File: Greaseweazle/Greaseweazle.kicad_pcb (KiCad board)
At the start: 2 copper layers, 90 x 94 mm, 20 parts, among them J1 FDC_PC, J2 PWR_EXT1, J3 PWR_DRV, J4 PWR_EXT2, J5 USB_TTL, J6 FDC_Amstrad, M1 Mounting, M2 Mounting, M3 Mounting, M4 Mounting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

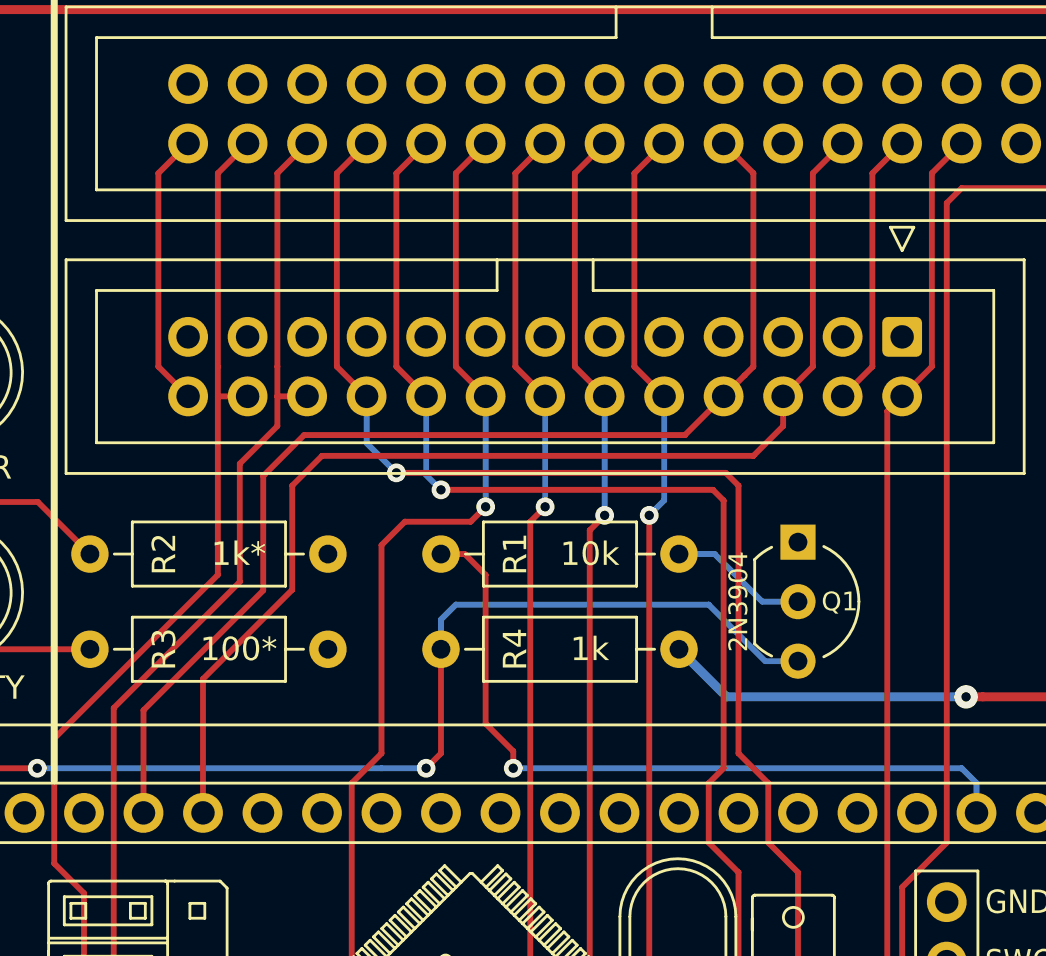
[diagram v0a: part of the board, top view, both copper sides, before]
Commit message: Tweaked Amstrad pinout to match pins available (still untested)
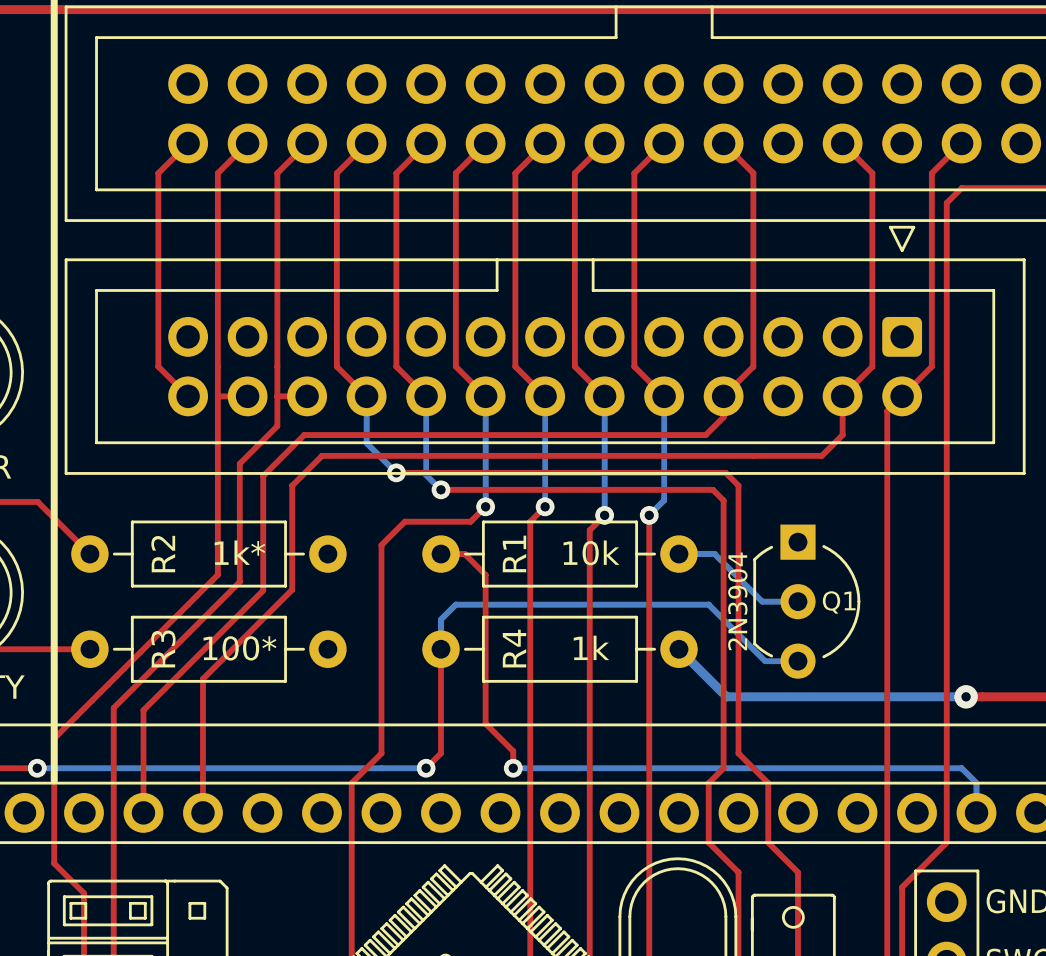
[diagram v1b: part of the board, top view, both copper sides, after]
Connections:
- J1 pad 10: /~MOTEA -> (no net)
- J6 pad 4: /~MOTEA -> /~DRVSB
- J6 pad 6: /~DRVSB -> (no net)
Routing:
- net /~MOTEA: track 11.8 -> 0.00 mm
- net /~DRVSB: track 50.7 -> 53.4 mm
- net /~MOTEB: track 49.4 -> 49.9 mm

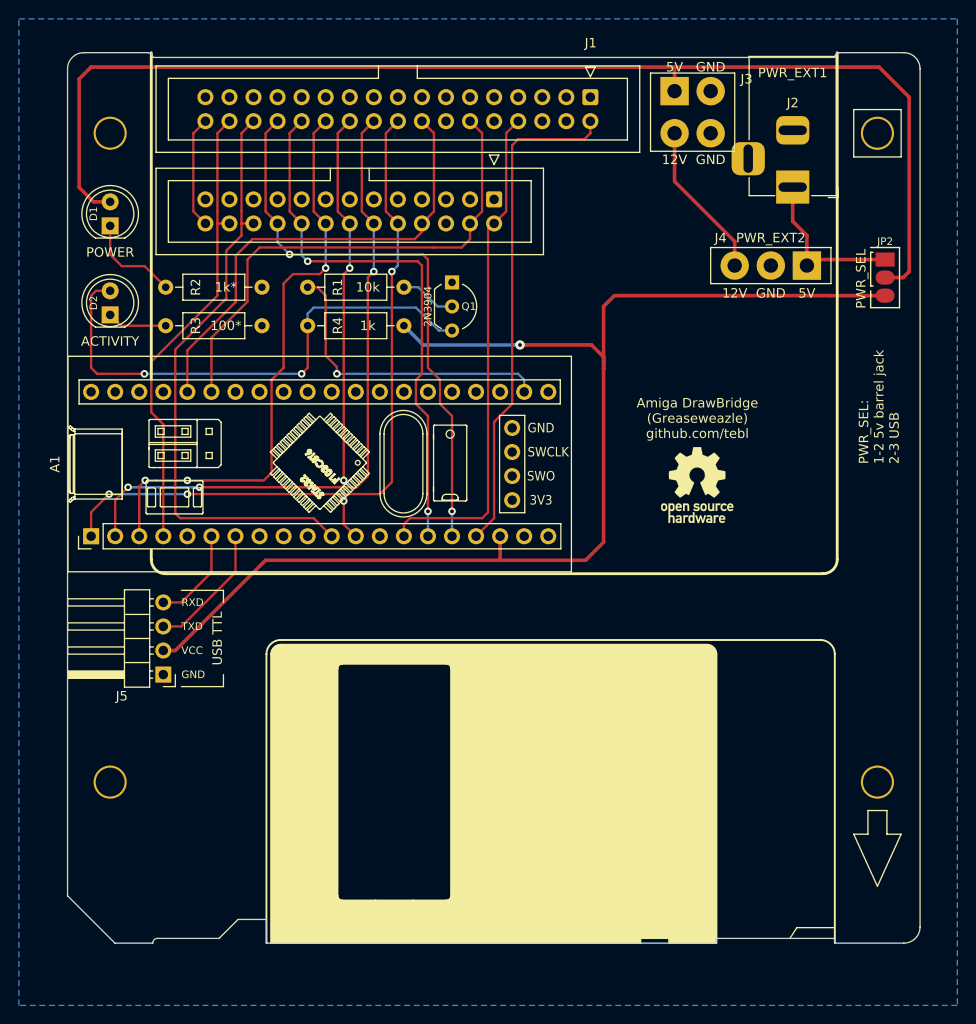
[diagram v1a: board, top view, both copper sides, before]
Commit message: Change PWR_EXT2 power input to 4pin
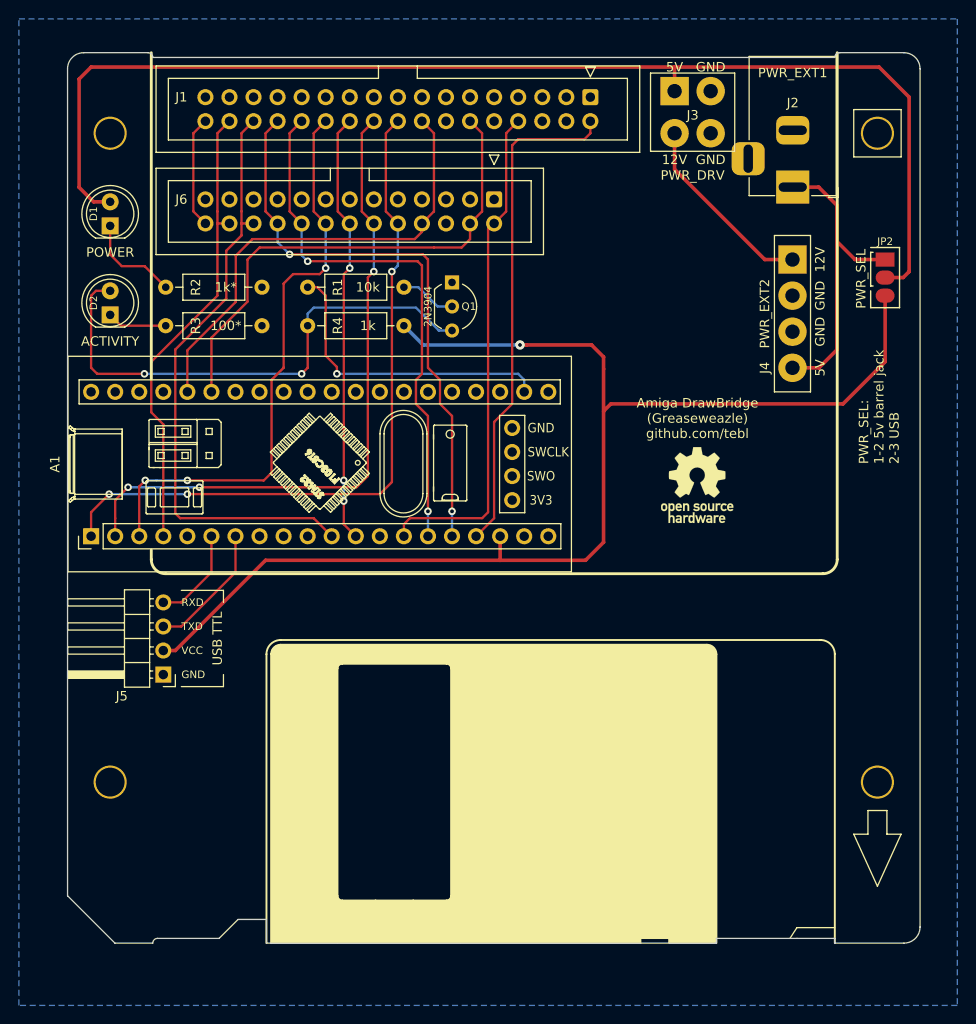
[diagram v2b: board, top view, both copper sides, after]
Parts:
- J4: footprint pwr_drv:PWR_EXT -> pwr_drv:PWR_IN
- moved J4 5.46 mm to (187.7, 80.6), turned to 90 degrees
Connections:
- J4 pad 1: Net-(J2-Pad1) -> Net-(J3-Pad4)
- J4 pad 3: Net-(J3-Pad4) -> GND
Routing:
- net Net-(J2-Pad1): track 17.4 -> 32.1 mm
- net Net-(J3-Pad4): track 16.6 -> 20.2 mm
- net VCC: track 132.6 -> 134.6 mm

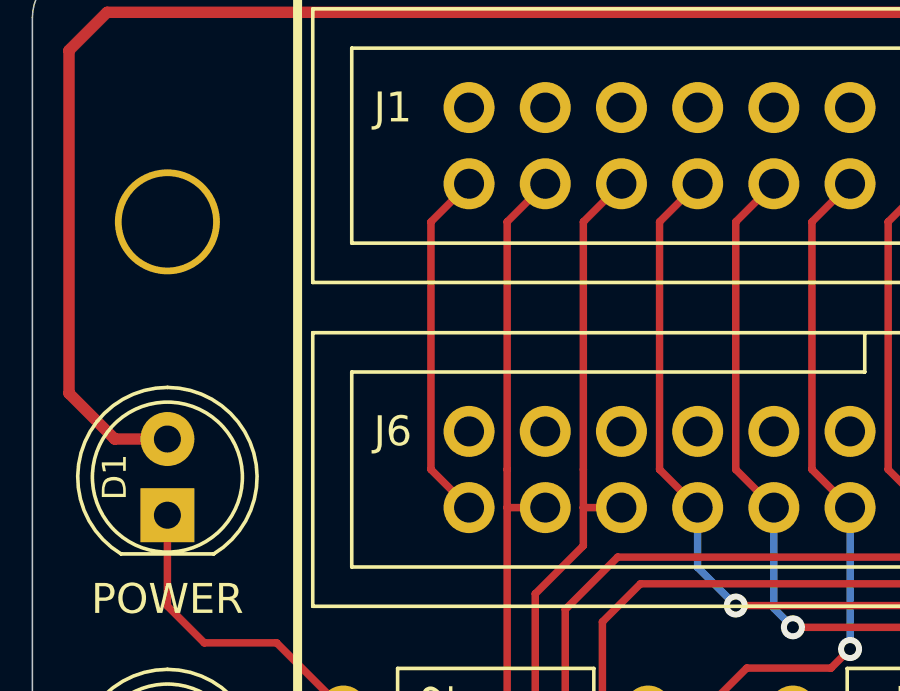
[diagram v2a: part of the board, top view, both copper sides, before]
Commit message: DKSCHG never actually connected to anything
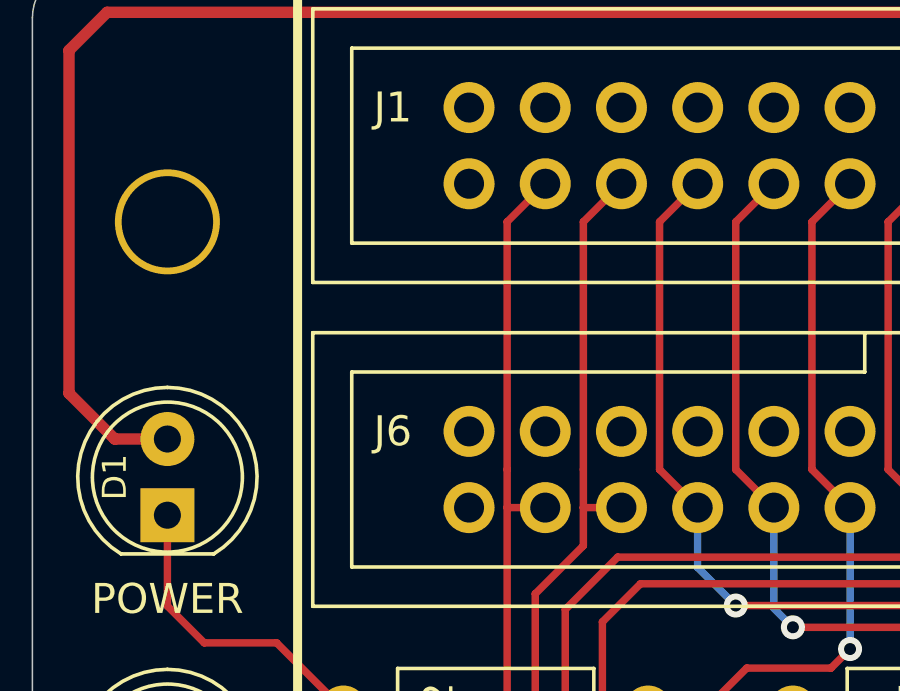
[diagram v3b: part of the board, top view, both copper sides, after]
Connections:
- J1 pad 34: /~DSKCHG -> (no net)
- J6 pad 26: /~DSKCHG -> (no net)
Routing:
- net /~DSKCHG: track 11.8 -> 0.00 mm

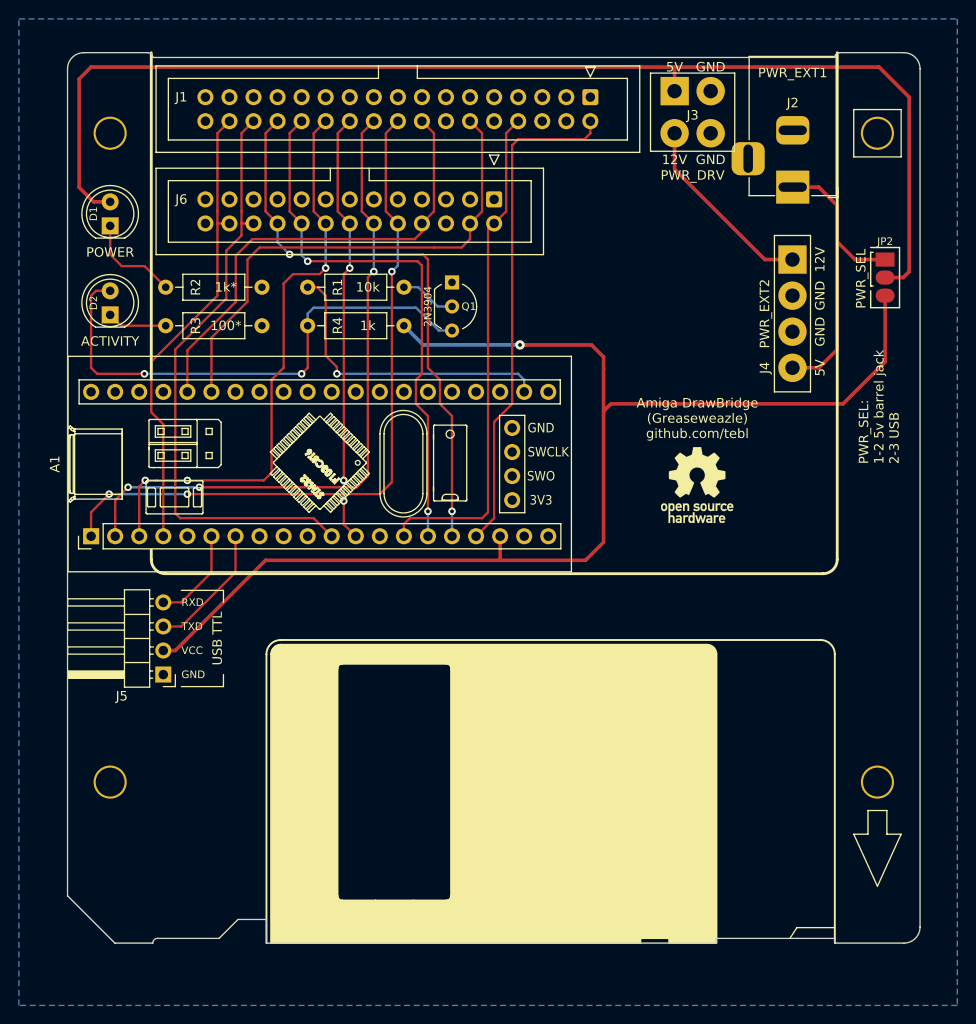
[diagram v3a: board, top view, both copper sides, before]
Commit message: Added pullups
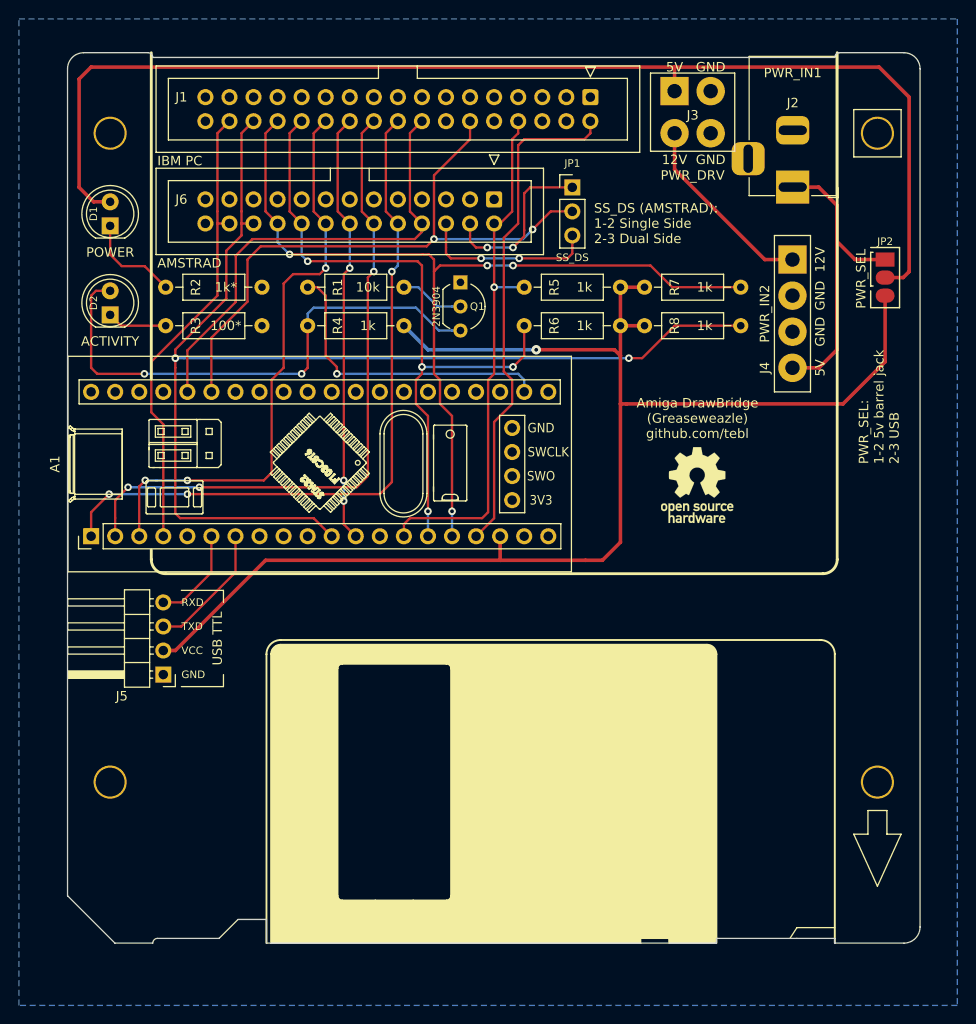
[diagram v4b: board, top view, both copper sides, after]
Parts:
- added JP1: SS_DS, Connector_PinHeader_2.54mm:PinHeader_1x03_P2.54mm_Vertical, F.Cu at (161.3, 69.2)
- added R5: 1k, Resistor_THT:R_Axial_DIN0207_L6.3mm_D2.5mm_P10.16mm_Horizontal, F.Cu at (166.4, 79.8)
- added R6: 1k, Resistor_THT:R_Axial_DIN0207_L6.3mm_D2.5mm_P10.16mm_Horizontal, F.Cu at (166.4, 83.8)
- added R7: 1k, Resistor_THT:R_Axial_DIN0207_L6.3mm_D2.5mm_P10.16mm_Horizontal, F.Cu at (168.9, 79.8)
- added R8: 1k, Resistor_THT:R_Axial_DIN0207_L6.3mm_D2.5mm_P10.16mm_Horizontal, F.Cu at (168.9, 83.8)
- J2: value PWR_EXT1 -> PWR_IN1
- J4: value PWR_EXT2 -> PWR_IN2
- moved Q1 0.89 mm to (149.5, 79.2)
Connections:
- J6 pad 4: /~DRVSB -> Net-(J6-Pad4)
- J6 pad 6: (no net) -> Net-(J6-Pad6)
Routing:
- net /~RDATA: track 63.6 -> 124.7 mm, vias 0 -> 2
- net /~WPT: track 60.7 -> 94.7 mm, vias 2 -> 4
- net Net-(J6-Pad6): track 0.00 -> 18.8 mm, vias 0 -> 2
- net Net-(J6-Pad4): track 0.00 -> 18.2 mm, vias 0 -> 2
- net /~TRK00: track 57.7 -> 72.2 mm, vias 2 -> 4
- net VCC: track 134.6 -> 148.5 mm
- net /~DRVSB: track 53.4 -> 66.0 mm, vias 0 -> 2
- net /~INDEX: track 53.3 -> 56.8 mm, vias 0 -> 1
- net Net-(Q1-Pad2): track 5.92 -> 6.81 mm
- net Net-(D2-Pad2): track 55.4 -> 56.3 mm
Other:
- board text added: "AMSTRAD"
- board text added: "IBM PC"
- board text added: "SS_DS (AMSTRAD): 1-2 Single Side 2-3 Dual Side"

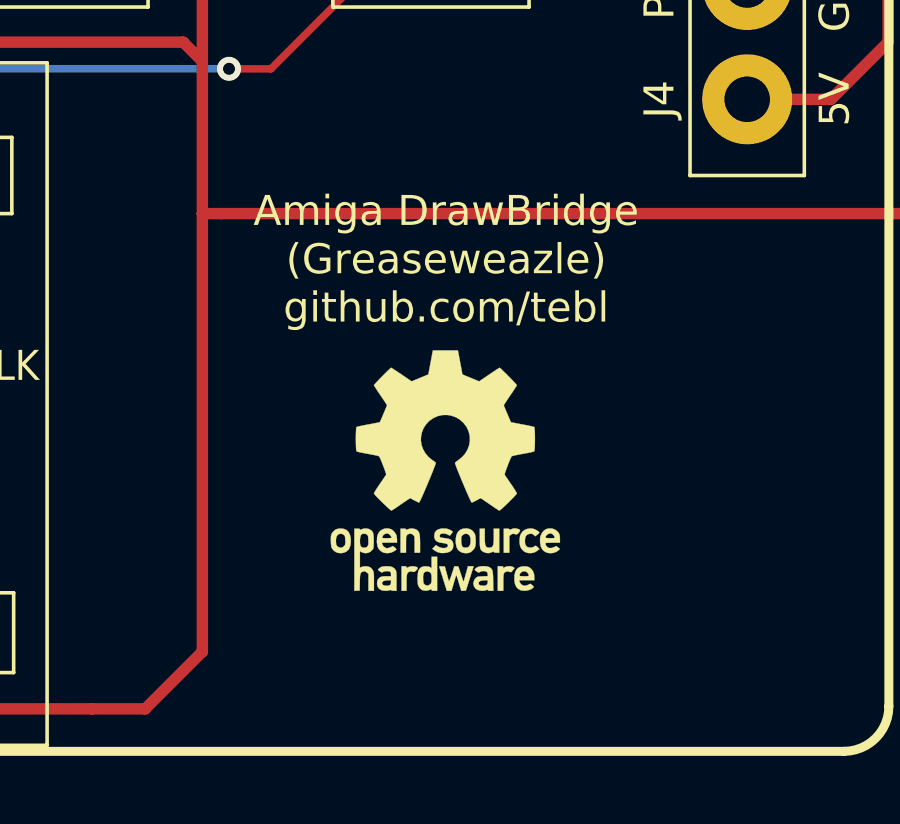
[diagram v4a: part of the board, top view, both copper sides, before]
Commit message: Silkscreen tweaks
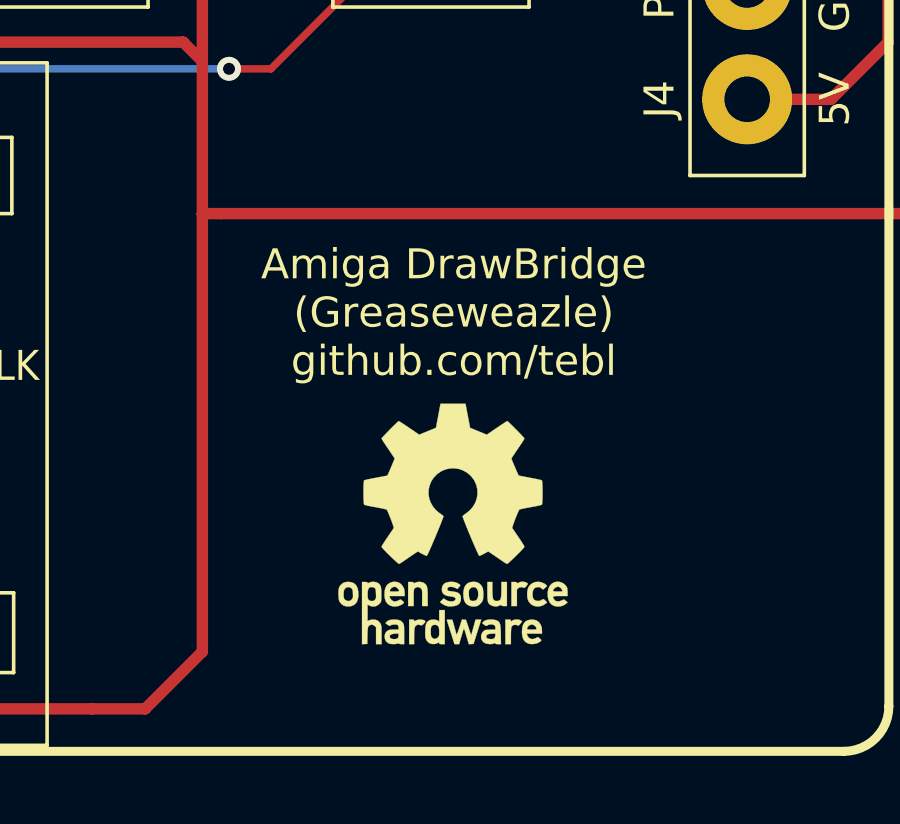
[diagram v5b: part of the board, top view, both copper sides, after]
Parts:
- moved REF** 1.80 mm to (174.7, 102.4)
